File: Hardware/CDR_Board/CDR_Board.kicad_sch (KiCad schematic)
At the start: 44 parts, among them J3 Battery, J4 Conn_ARM_JTAG_SWD_10, J5 USB_C_Receptacle_USB2.0, Q1 DMP2045U, SW1 SW_Push, SW2 SW_Push, U1 W25Q32JVSS, U2 SOT23-5 200mA 3.3V, U3 RP2040, U4 MCP73831-2-OT, Y1 Crystal

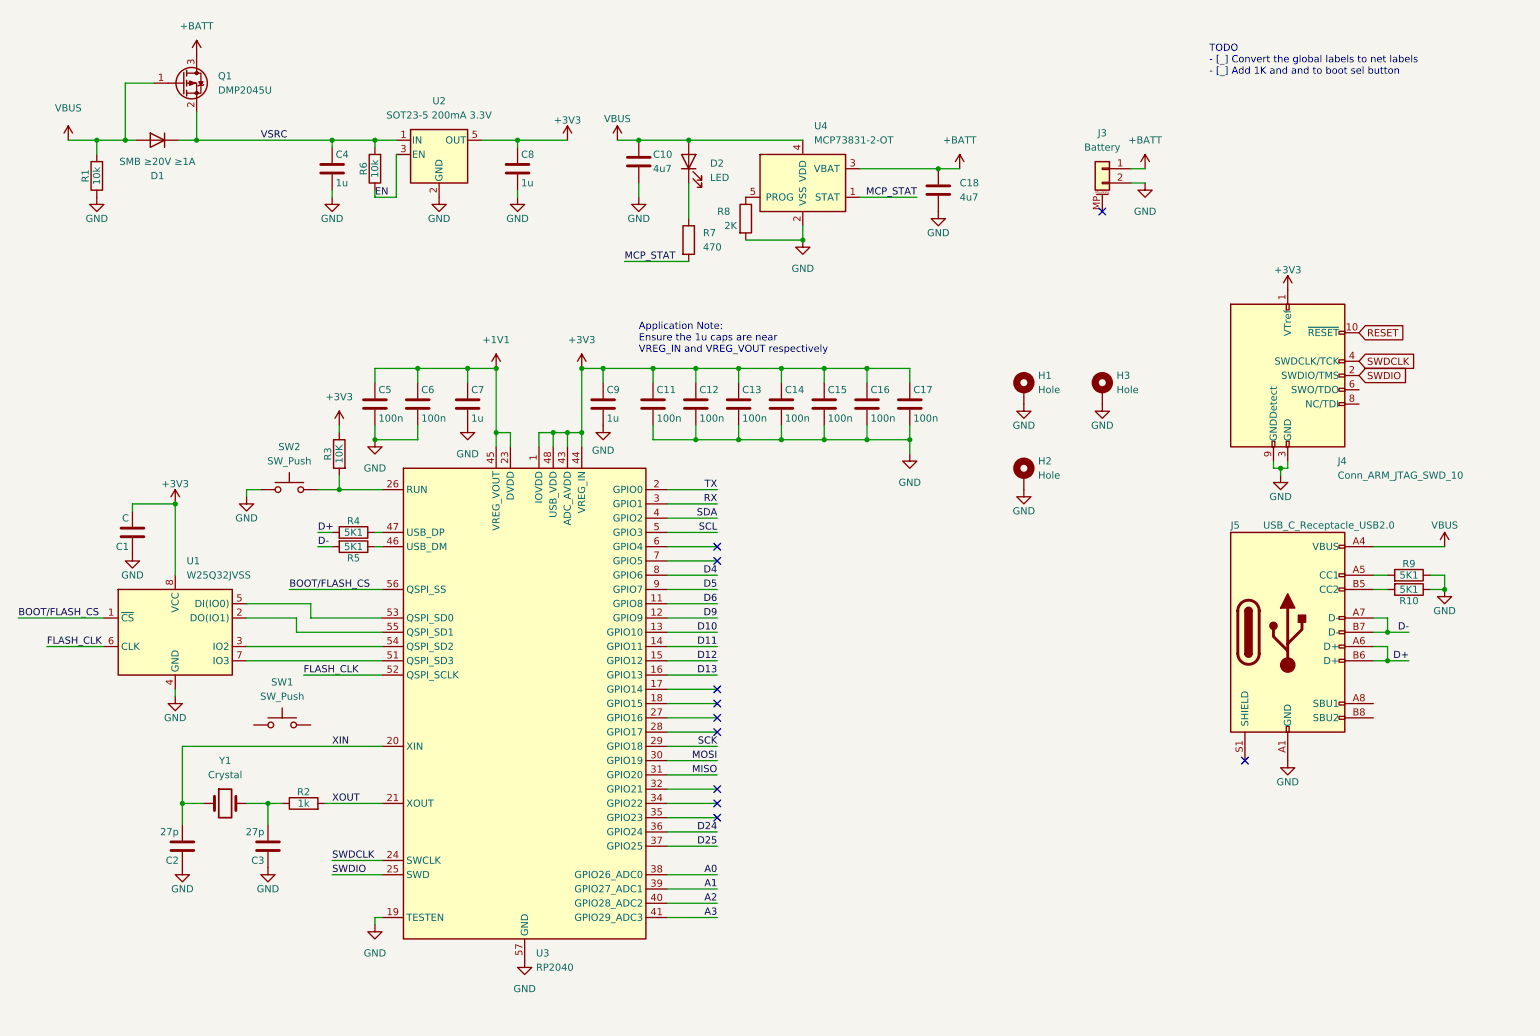
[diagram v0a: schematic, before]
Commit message: CDR Board Component Placement
Component placement on 50 mil grid.
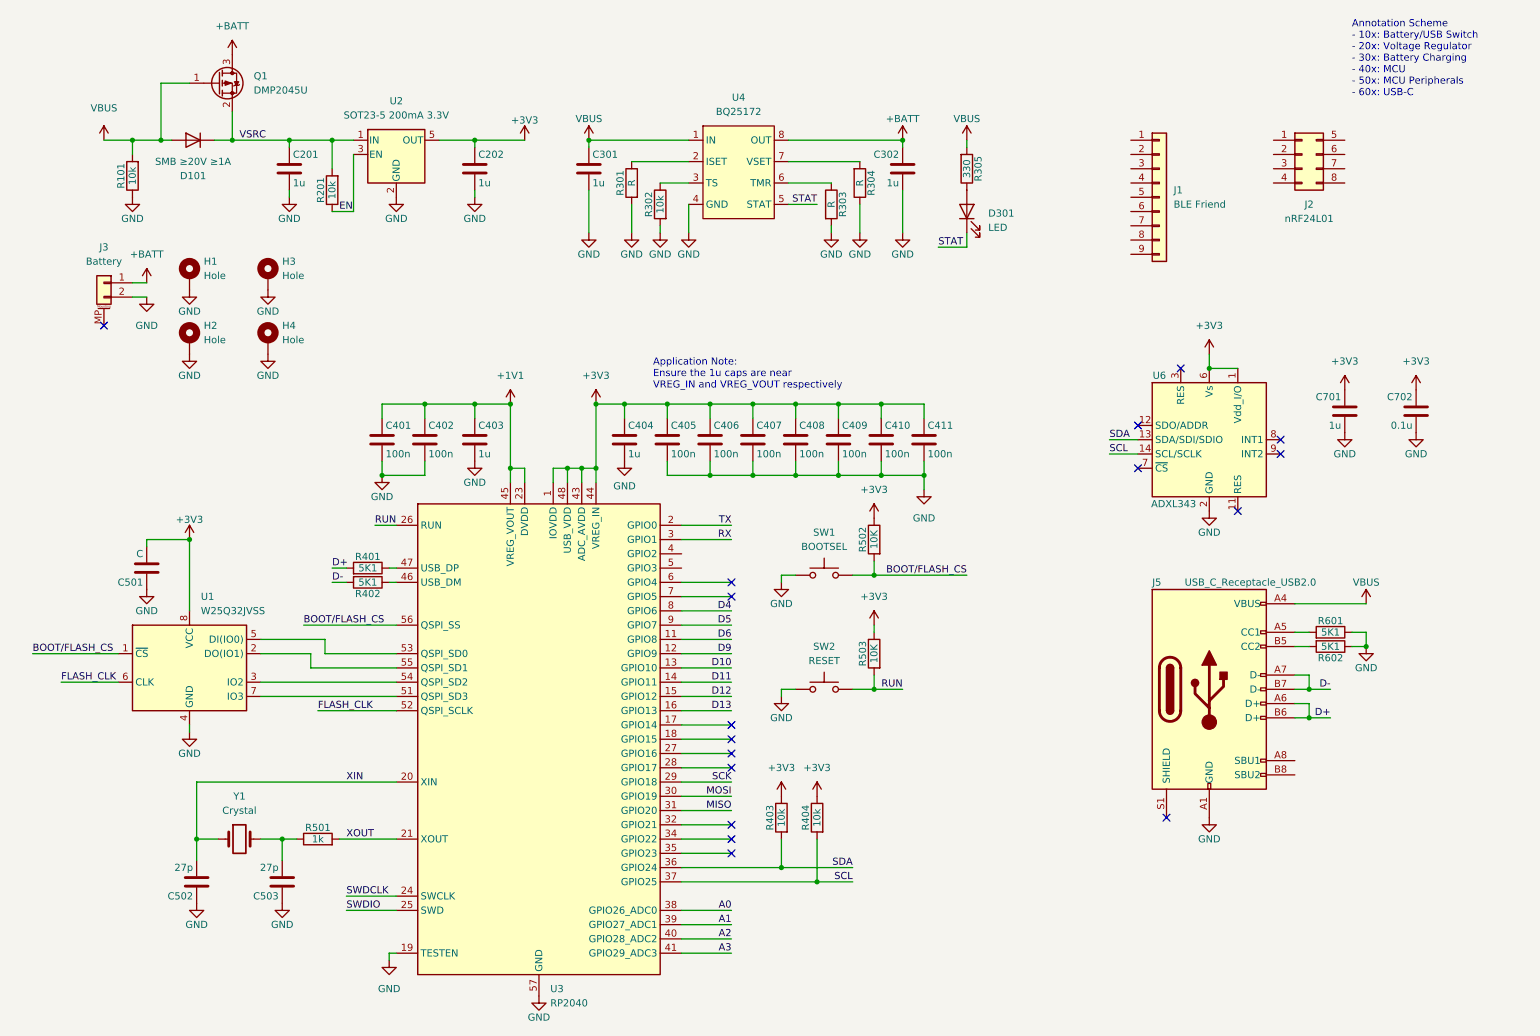
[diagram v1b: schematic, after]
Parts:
- removed C10, C18: 4u7, Capacitor_SMD:C_0805_2012Metric_Pad1.18x1.45mm_HandSolder, symbol Device:C
- removed D2: LED, LED_SMD:LED_0805_2012Metric_Pad1.15x1.40mm_HandSolder, symbol Device:LED
- removed J4: Conn_ARM_JTAG_SWD_10, Connector_PinHeader_1.27mm:PinHeader_2x05_P1.27mm_Vertical_SMD, symbol Connector:Conn_ARM_JTAG_SWD_10
- removed R3: 10K, Resistor_SMD:R_0805_2012Metric_Pad1.20x1.40mm_HandSolder, symbol Device:R
- removed R7: 470, Resistor_SMD:R_0805_2012Metric_Pad1.20x1.40mm_HandSolder, symbol Device:R
- removed R8: 2K, Resistor_SMD:R_0805_2012Metric_Pad1.20x1.40mm_HandSolder, symbol Device:R
- removed U4: MCP73831-2-OT, Package_TO_SOT_SMD:SOT-23-5, symbol Battery_Management:MCP73831-2-OT
- added C301, C302, C701: 1u, Capacitor_SMD:C_0805_2012Metric_Pad1.18x1.45mm_HandSolder, symbol Device:C
- added C702: 0.1u, Capacitor_SMD:C_0805_2012Metric_Pad1.18x1.45mm_HandSolder, symbol Device:C
- added D301: LED, LED_SMD:LED_0805_2012Metric_Pad1.15x1.40mm_HandSolder, symbol Device:LED
- added H4: Hole, MountingHole:MountingHole_2.2mm_M2_DIN965_Pad, symbol Mechanical:MountingHole_Pad
- added J1: BLE Friend, Connector_PinSocket_2.54mm:PinSocket_1x09_P2.54mm_Vertical, symbol Connector_Generic:Conn_01x09
- added J2: nRF24L01, Connector_PinSocket_2.54mm:PinSocket_2x04_P2.54mm_Vertical, symbol Connector_Generic:Conn_02x04_Top_Bottom
- added R301, R303, R304: R, Resistor_SMD:R_0805_2012Metric_Pad1.20x1.40mm_HandSolder, symbol Device:R
- added R302, R403, R404: 10k, Resistor_SMD:R_0805_2012Metric_Pad1.20x1.40mm_HandSolder, symbol Device:R
- added R305: 330, Resistor_SMD:R_0805_2012Metric_Pad1.20x1.40mm_HandSolder, symbol Device:R
- added R502, R503: 10K, Resistor_SMD:R_0805_2012Metric_Pad1.20x1.40mm_HandSolder, symbol Device:R
- added U4: BQ25172, Package_SON:WSON-8-1EP_2x2mm_P0.5mm_EP0.9x1.6mm_ThermalVias, symbol NiMH_Charger:BQ25172
- added U6: ADXL343, Package_LGA:LGA-14_3x5mm_P0.8mm_LayoutBorder1x6y, symbol Sensor_Motion:ADXL343
- SW1: value SW_Push -> BOOTSEL
- SW2: value SW_Push -> RESET
- U3: footprint Package_DFN_QFN:QFN-56-1EP_7x7mm_P0.4mm_EP3.2x3.2mm -> Package_DFN_QFN:QFN-56-1EP_7x7mm_P0.4mm_EP3.2x3.2mm_ThermalVias
- renumbered C4 to C201, C8 to C202, C5 to C401, C6 to C402, C7 to C403, C9 to C404, C11 to C405, C12 to C406, C13 to C407, C14 to C408, C15 to C409, C16 to C410, C17 to C411, C1 to C501, C2 to C502, C3 to C503, D1 to D101, R1 to R101, R6 to R201, R4 to R401, R5 to R402, R2 to R501, R9 to R601, R10 to R602
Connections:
- net D24 is gone; now on net SDA: U3.36 (GPIO24)
- net D25 is gone; now on net SCL: U3.37 (GPIO25)
- net +3V3: now also C701.1, C702.1, R403.1, R404.1, R502.1, R503.1, U6.1 (Vdd_I/O), U6.6 (Vs)
- net +BATT: now also C302.1, U4.8 (OUT)
- net BOOT/FLASH_CS: now also SW1.2, R502.2
- net GND: now also SW1.1, C301.2, C302.2, C701.2, C702.2, H4.1, R301.2, R302.2, R303.2, R304.1, U4.4 (GND), U6.2 (GND), U6.4 (GND), U6.5 (GND)
- net SCL: now also R404.2, U6.14 (SCL/SCLK); no longer U3.5 (GPIO3)
- net SDA: now also R403.2, U6.13 (SDA/SDI/SDIO); no longer U3.4 (GPIO2)
- net VBUS: now also C301.1, R305.2, U4.1 (IN)
- net RUN: now reaches SW2.2, U3.26 (RUN)
- net RUN: now also R503.2
- new net: D301.2 (A), R305.1
- new net: R303.1, U4.6 (TMR)
- new net: R304.2, U4.7 (VSET)
- new net: R301.1, U4.2 (ISET)
- new net: R302.1, U4.3 (TS)
- new net STAT: D301.1 (K), U4.5 (STAT)
- no-connect marks 11 -> 17
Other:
- note added: "Annotation Scheme - 10x: Battery/USB Switch - 20x: Voltage Regulator - 30x: Battery Charging - 40x: MCU - 50x: MCU Peripherals - 60x: USB-C"
- note removed: "TODO - [_] Convert the global labels to net labels - [_] Add 1K and and to boot sel button"
- moved on the sheet: C201, C202, C401, C402, C403, C404, C405, C406, C407, C408, C409, C410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

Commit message: CDR Board Placement Revision
Some things on 25 mil grid, 0603 capacitors for RP2040 decoupling.
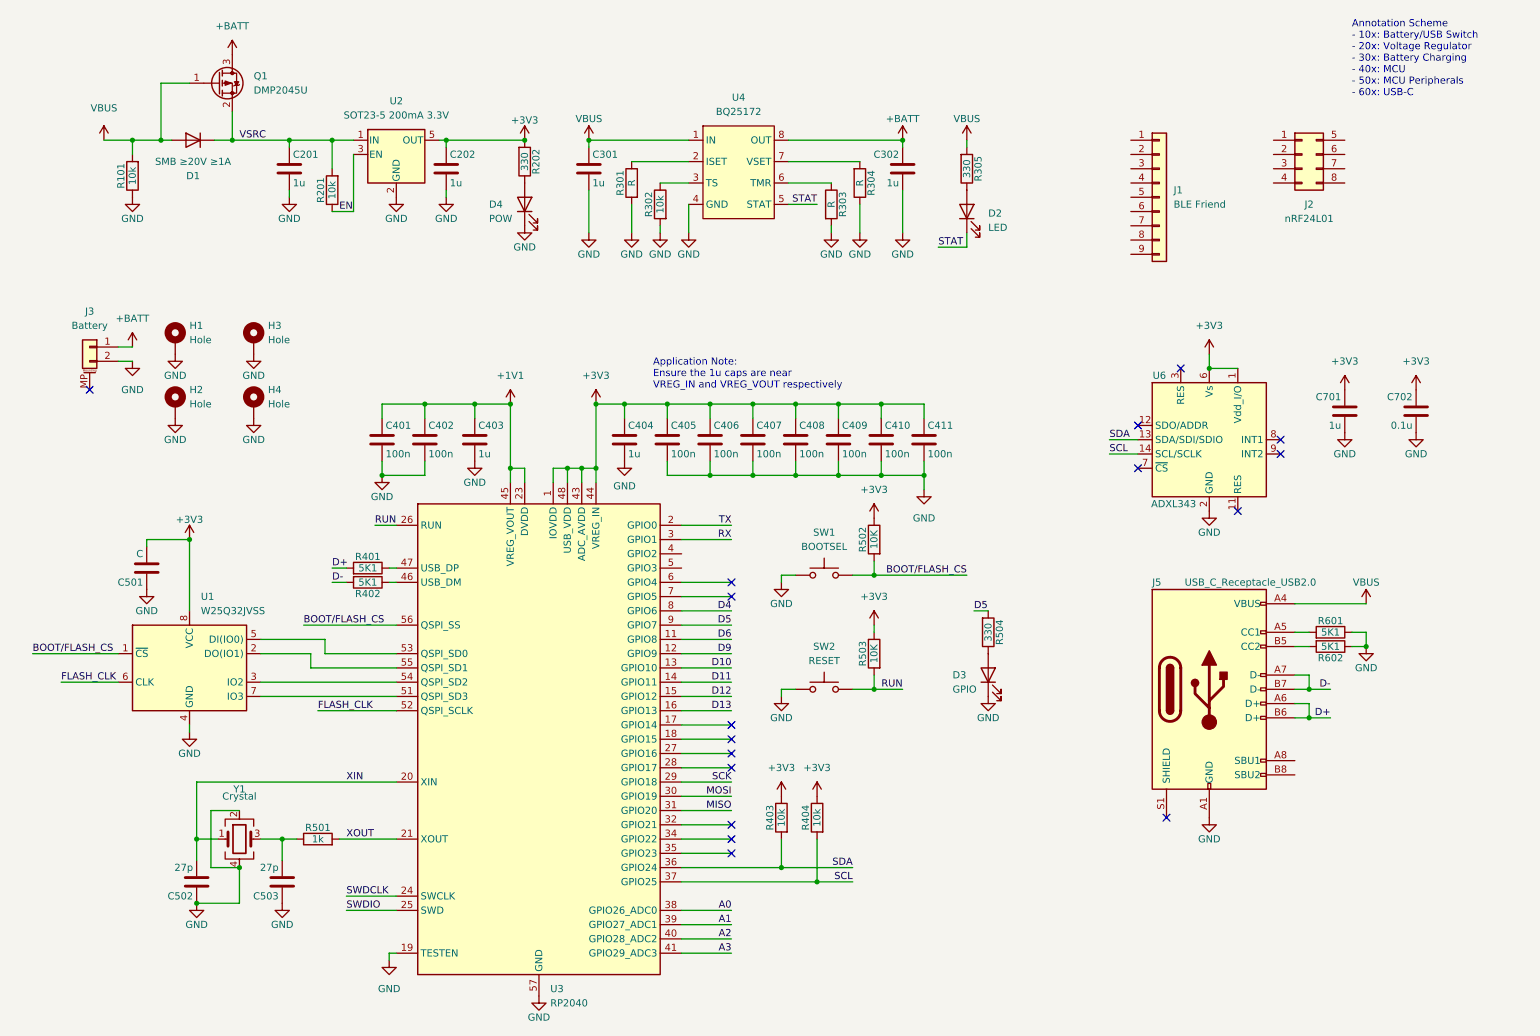
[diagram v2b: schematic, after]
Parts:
- removed Y1: Crystal, Crystal:Crystal_SMD_Abracon_ABM3-2Pin_5.0x3.2mm_HandSoldering, symbol Device:Crystal
- added D3: GPIO, LED_SMD:LED_0805_2012Metric_Pad1.15x1.40mm_HandSolder, symbol Device:LED
- added D4: POW, LED_SMD:LED_0805_2012Metric_Pad1.15x1.40mm_HandSolder, symbol Device:LED
- added R202, R504: 330, Resistor_SMD:R_0805_2012Metric_Pad1.20x1.40mm_HandSolder, symbol Device:R
- added Y1: Crystal, Crystal:Crystal_SMD_SeikoEpson_FA238-4Pin_3.2x2.5mm, symbol Device:Crystal_GND24
- C401, C402, C403, C404, C405, C406, C407, C408, C409, C410, C411: footprint Capacitor_SMD:C_0805_2012Metric_Pad1.18x1.45mm_HandSolder -> Capacitor_SMD:C_0603_1608Metric_Pad1.08x0.95mm_HandSolder
- renumbered D101 to D1, D301 to D2
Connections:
- net +3V3: now also R202.2
- net D5: now also R504.2
- net GND: now also D3.1 (K), D4.1 (K), Y1.2, Y1.4
- net XIN: now also Y1.1
- net at C503.2, R501.1: now also Y1.3
- new net: D4.2 (A), R202.1
- new net: D3.2 (A), R504.1
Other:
- moved on the sheet: C202, H1, H2, H3, H4, J3
